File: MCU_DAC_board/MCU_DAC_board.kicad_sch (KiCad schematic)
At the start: 50 parts, among them J11 105-0752-001, J5 54-00127, J6 105-0752-001, J7 Screw_Terminal_01x02, J8 Screw_Terminal_01x02, J9 Conn_02x20_Odd_Even, Q1 FZT953, U1 ADAU1966AWBSTZ

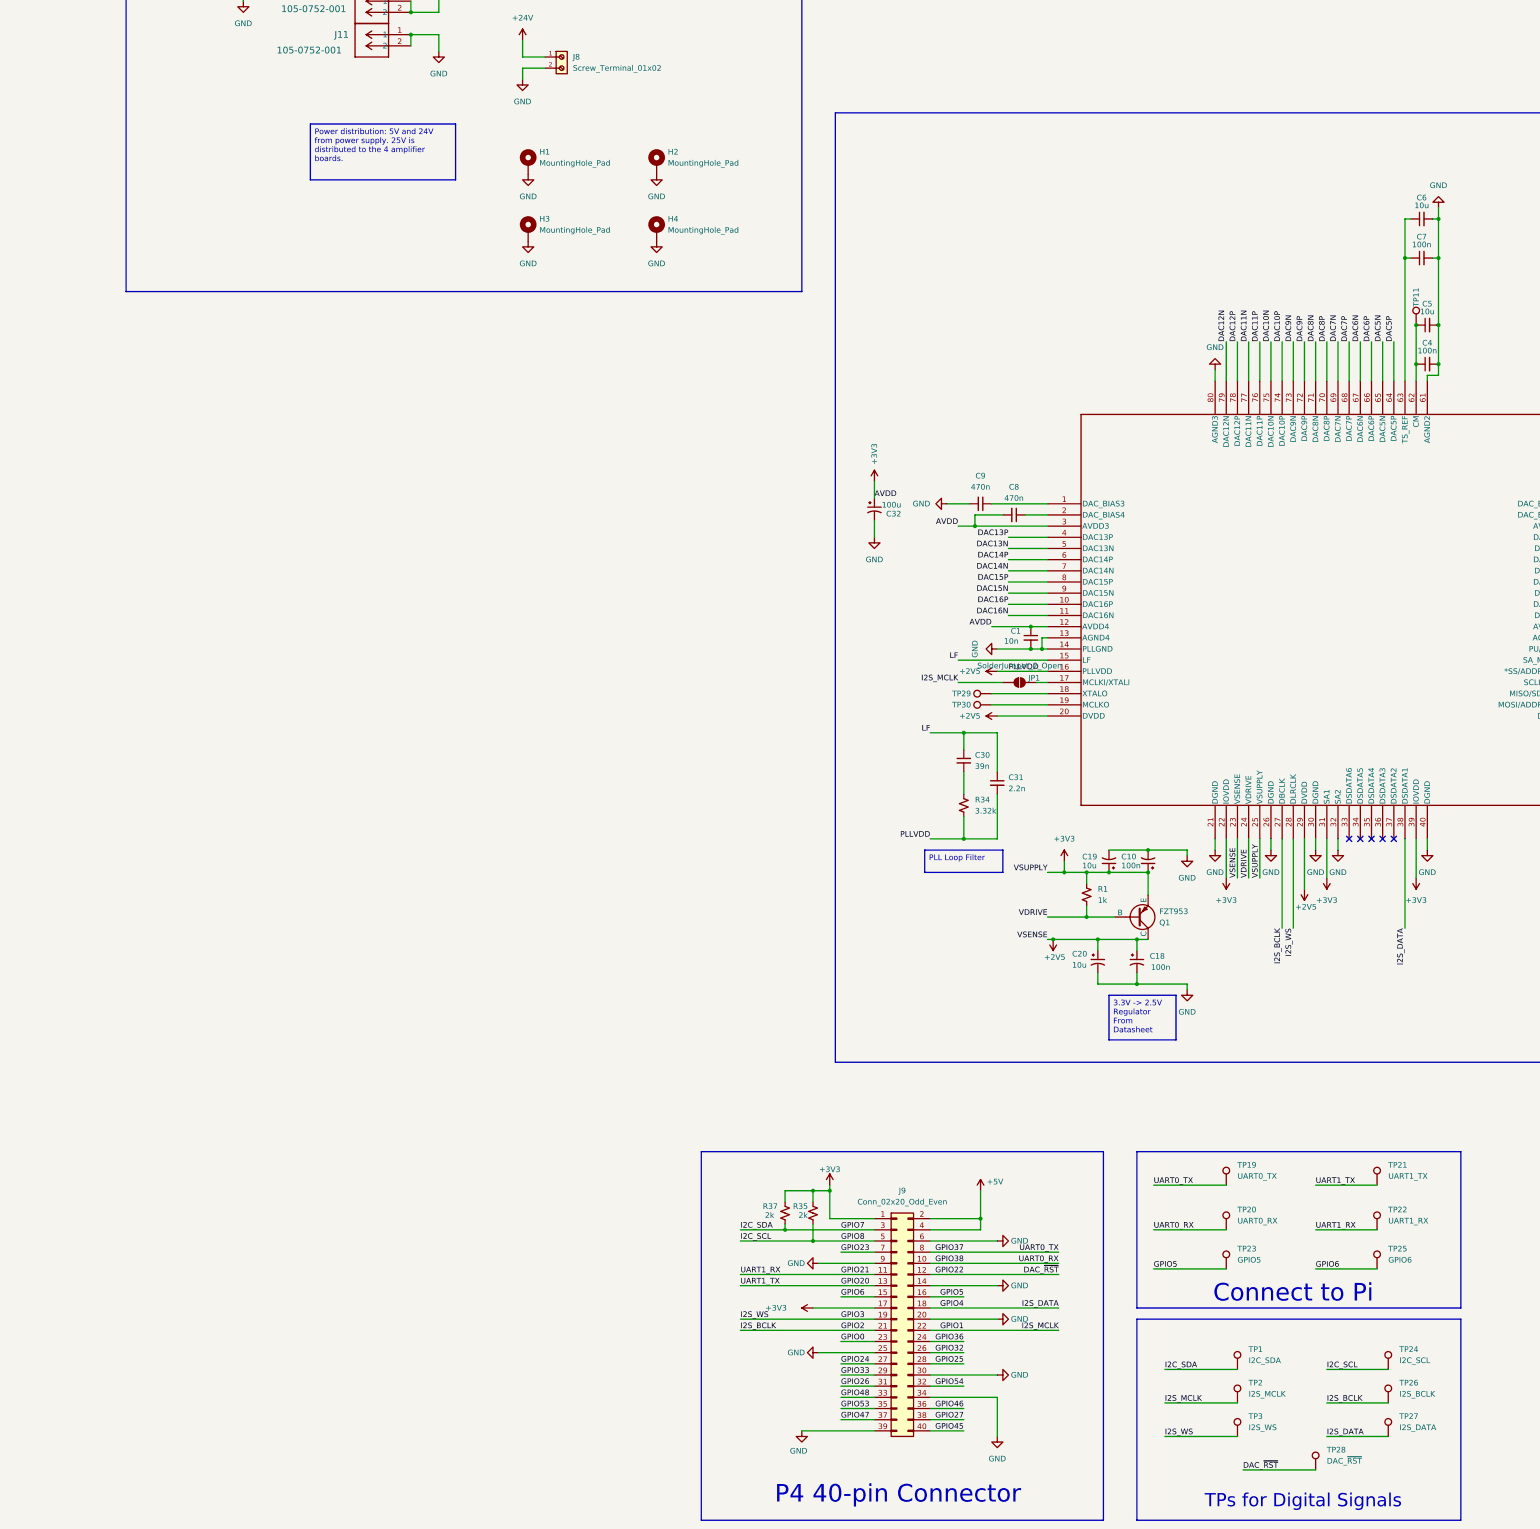
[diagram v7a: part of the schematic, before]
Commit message: Added DIP conector for UART connections
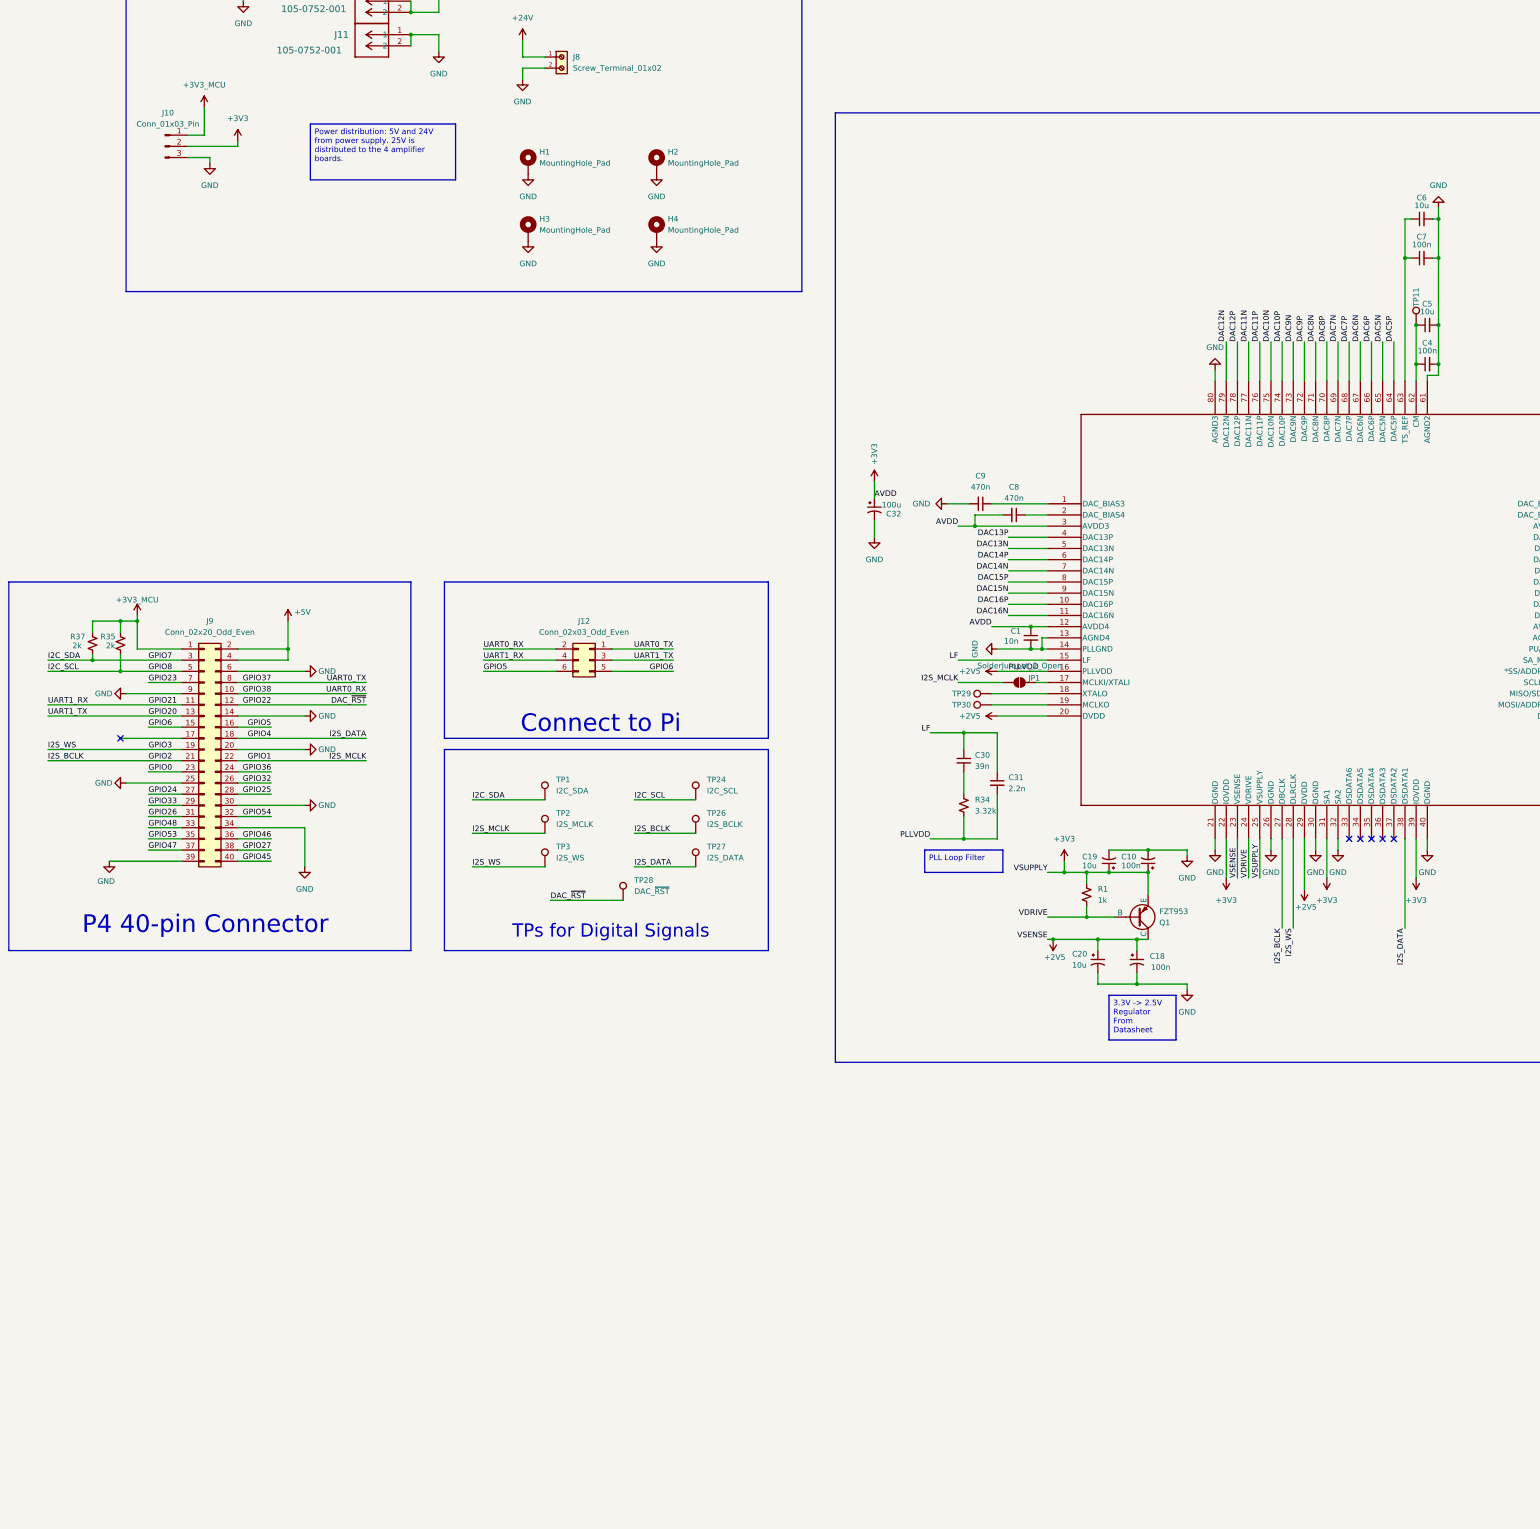
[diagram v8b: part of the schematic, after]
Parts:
- removed TP19: UART0_TX, project_lib:TP_1.8x1mm, symbol Connector:TestPoint
- removed TP20: UART0_RX, project_lib:TP_1.8x1mm, symbol Connector:TestPoint
- removed TP21: UART1_TX, project_lib:TP_1.8x1mm, symbol Connector:TestPoint
- removed TP22: UART1_RX, project_lib:TP_1.8x1mm, symbol Connector:TestPoint
- removed TP23: GPIO5, project_lib:TP_1.8x1mm, symbol Connector:TestPoint
- removed TP25: GPIO6, project_lib:TP_1.8x1mm, symbol Connector:TestPoint
- added J10: Conn_01x03_Pin, Connector_PinHeader_2.54mm:PinHeader_1x03_P2.54mm_Vertical, symbol Connector:Conn_01x03_Pin
- added J12: Conn_02x03_Odd_Even, Connector_PinSocket_2.54mm:PinSocket_2x03_P2.54mm_Vertical, symbol Connector_Generic:Conn_02x03_Odd_Even
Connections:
- net +3V3: now also J10.2 (Pin_2); no longer J9.1 (Pin_1), J9.17 (Pin_17), R35.1, R37.1
- net GND: now also J10.3 (Pin_3)
- net GPIO20: now also J12.3 (Pin_3)
- net GPIO21: now also J12.4 (Pin_4)
- net GPIO37: now also J12.1 (Pin_1)
- net GPIO38: now also J12.2 (Pin_2)
- net GPIO5: now also J12.6 (Pin_6)
- net GPIO6: now also J12.5 (Pin_5)
- new net +3V3_MCU: J10.1 (Pin_1), J9.1 (Pin_1), R35.1, R37.1
- no-connect marks 6 -> 7
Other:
- moved on the sheet: J9, R35, R37, TP1, TP2, TP24, TP26, TP27, TP28, TP3
